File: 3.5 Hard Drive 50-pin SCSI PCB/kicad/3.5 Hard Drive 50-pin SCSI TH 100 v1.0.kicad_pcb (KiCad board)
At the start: 2 copper layers, 100 x 94.4 mm, 3 parts, among them J1 IDC-Header_2x25_P2.54mm_Horiz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, J2 TE_MATE-N-LOK_ 770846-1_1x04_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

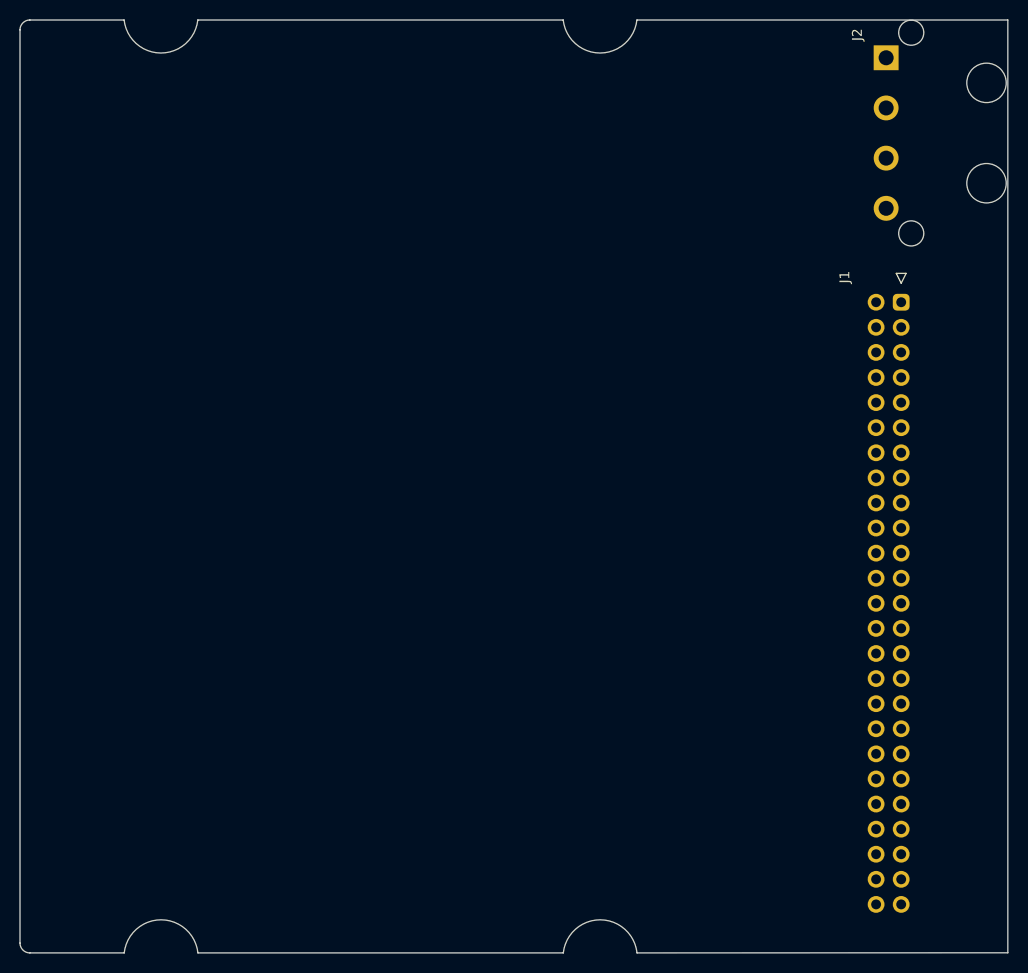
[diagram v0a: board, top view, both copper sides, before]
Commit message: Update to Kicad 6.
Share Kicad symbols and footprints across all projects.
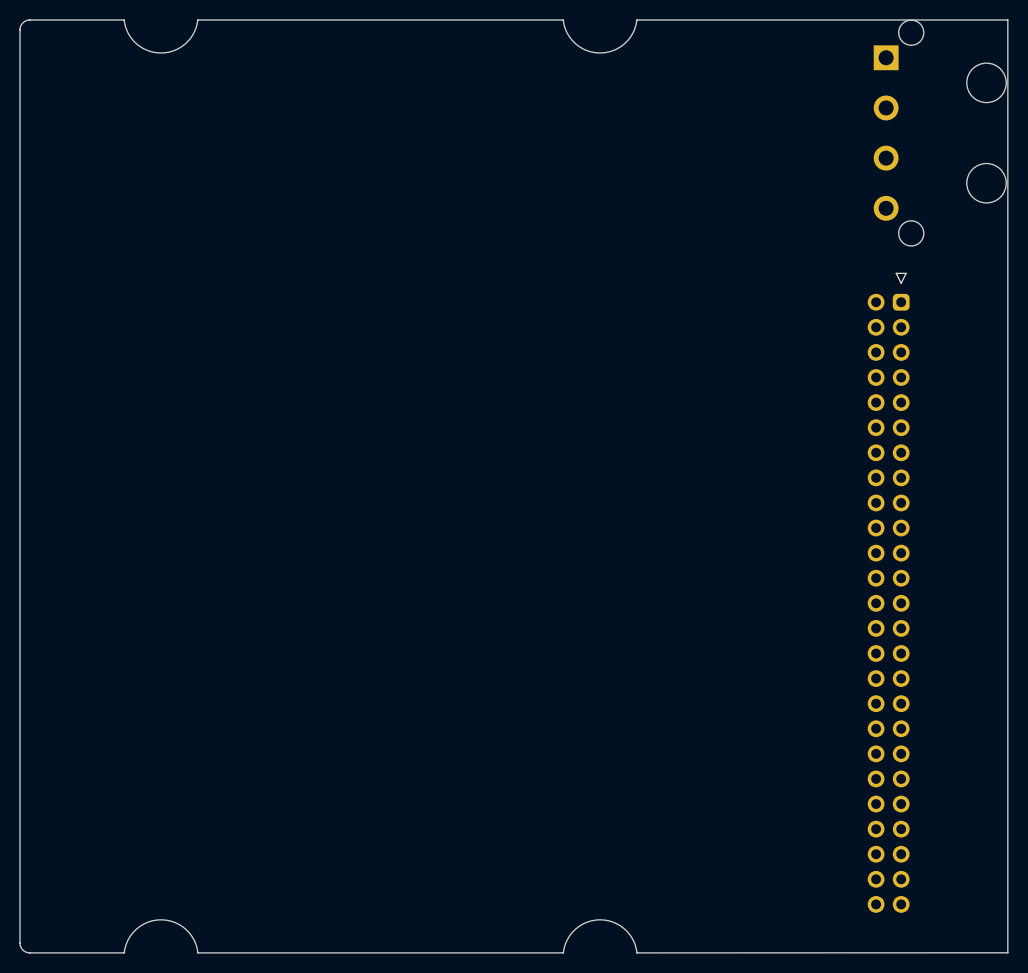
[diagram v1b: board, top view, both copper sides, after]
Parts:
- J1: value IDC-Header_2x25_P2.54mm_Horizontal_Under -> SCSI_SE_Internal_Conn_02x25_Odd_Even_MountingPin-Macintosh_Portable_50-pin_Hard_Drive_Adapter
- J2: value TE_MATE-N-LOK_ 770846-1_1x04_P5.08mm_horizontal -> Hard_Drive_Mate_n-Lok_Power_Conn_01x04; footprint project:TE_MATE-N-LOK_770846-1_1x04_P5.08mm_Horizontal -> project:TE_MATE-N-LOK_770846-1_1x04_P5.08mm_Horizontal_Under; moved to F.Cu
- turned J2 to 0 degrees
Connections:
- J1 pad 1: (no net) -> unconnected-(J1-Pad1)
- J1 pad 10: (no net) -> unconnected-(J1-Pad10)
- J1 pad 11: (no net) -> unconnected-(J1-Pad11)
- J1 pad 12: (no net) -> unconnected-(J1-Pad12)
- J1 pad 13: (no net) -> unconnected-(J1-Pad13)
- J1 pad 14: (no net) -> unconnected-(J1-Pad14)
- J1 pad 15: (no net) -> unconnected-(J1-Pad15)
- J1 pad 16: (no net) -> unconnected-(J1-Pad16)
- J1 pad 17: (no net) -> unconnected-(J1-Pad17)
- J1 pad 18: (no net) -> unconnected-(J1-Pad18)
- J1 pad 19: (no net) -> unconnected-(J1-Pad19)
- J1 pad 2: (no net) -> unconnected-(J1-Pad2)
- J1 pad 20: (no net) -> unconnected-(J1-Pad20)
- J1 pad 21: (no net) -> unconnected-(J1-Pad21)
- J1 pad 22: (no net) -> unconnected-(J1-Pad22)
- J1 pad 23: (no net) -> unconnected-(J1-Pad23)
- J1 pad 24: (no net) -> unconnected-(J1-Pad24)
- J1 pad 25: (no net) -> unconnected-(J1-Pad25)
- J1 pad 26: (no net) -> unconnected-(J1-Pad26)
- J1 pad 27: (no net) -> unconnected-(J1-Pad27)
- J1 pad 28: (no net) -> unconnected-(J1-Pad28)
- J1 pad 29: (no net) -> unconnected-(J1-Pad29)
- J1 pad 3: (no net) -> unconnected-(J1-Pad3)
- J1 pad 30: (no net) -> unconnected-(J1-Pad30)
- J1 pad 31: (no net) -> unconnected-(J1-Pad31)
- J1 pad 32: (no net) -> unconnected-(J1-Pad32)
- J1 pad 33: (no net) -> unconnected-(J1-Pad33)
- J1 pad 34: (no net) -> unconnected-(J1-Pad34)
- J1 pad 35: (no net) -> unconnected-(J1-Pad35)
- J1 pad 36: (no net) -> unconnected-(J1-Pad36)
- J1 pad 37: (no net) -> unconnected-(J1-Pad37)
- J1 pad 38: (no net) -> unconnected-(J1-Pad38)
- J1 pad 39: (no net) -> unconnected-(J1-Pad39)
- J1 pad 4: (no net) -> unconnected-(J1-Pad4)
- J1 pad 40: (no net) -> unconnected-(J1-Pad40)
- J1 pad 41: (no net) -> unconnected-(J1-Pad41)
- J1 pad 42: (no net) -> unconnected-(J1-Pad42)
- J1 pad 43: (no net) -> unconnected-(J1-Pad43)
- J1 pad 44: (no net) -> unconnected-(J1-Pad44)
- J1 pad 45: (no net) -> unconnected-(J1-Pad45)
- J1 pad 46: (no net) -> unconnected-(J1-Pad46)
- J1 pad 47: (no net) -> unconnected-(J1-Pad47)
- J1 pad 48: (no net) -> unconnected-(J1-Pad48)
- J1 pad 49: (no net) -> unconnected-(J1-Pad49)
- J1 pad 5: (no net) -> unconnected-(J1-Pad5)
- J1 pad 50: (no net) -> unconnected-(J1-Pad50)
- J1 pad 6: (no net) -> unconnected-(J1-Pad6)
- J1 pad 7: (no net) -> unconnected-(J1-Pad7)
- J1 pad 8: (no net) -> unconnected-(J1-Pad8)
- J1 pad 9: (no net) -> unconnected-(J1-Pad9)
- J2 pad 1: (no net) -> unconnected-(J2-Pad1)
- J2 pad 2: (no net) -> unconnected-(J2-Pad2)
- J2 pad 3: (no net) -> unconnected-(J2-Pad3)
- J2 pad 4: (no net) -> unconnected-(J2-Pad4)
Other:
- net class Default removed
